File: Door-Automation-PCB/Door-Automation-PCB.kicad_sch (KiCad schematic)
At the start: 10 parts, among them J1 Conn_01x15_Female, J2 Conn_01x15_Female, J3 Screw_Terminal_01x01, J4 Screw_Terminal_01x01, J5 Screw_Terminal_01x02, J6 Screw_Terminal_01x02, U1 ESP32-DEVKIT-V1, U2 buck_converter, U3 buck_converter

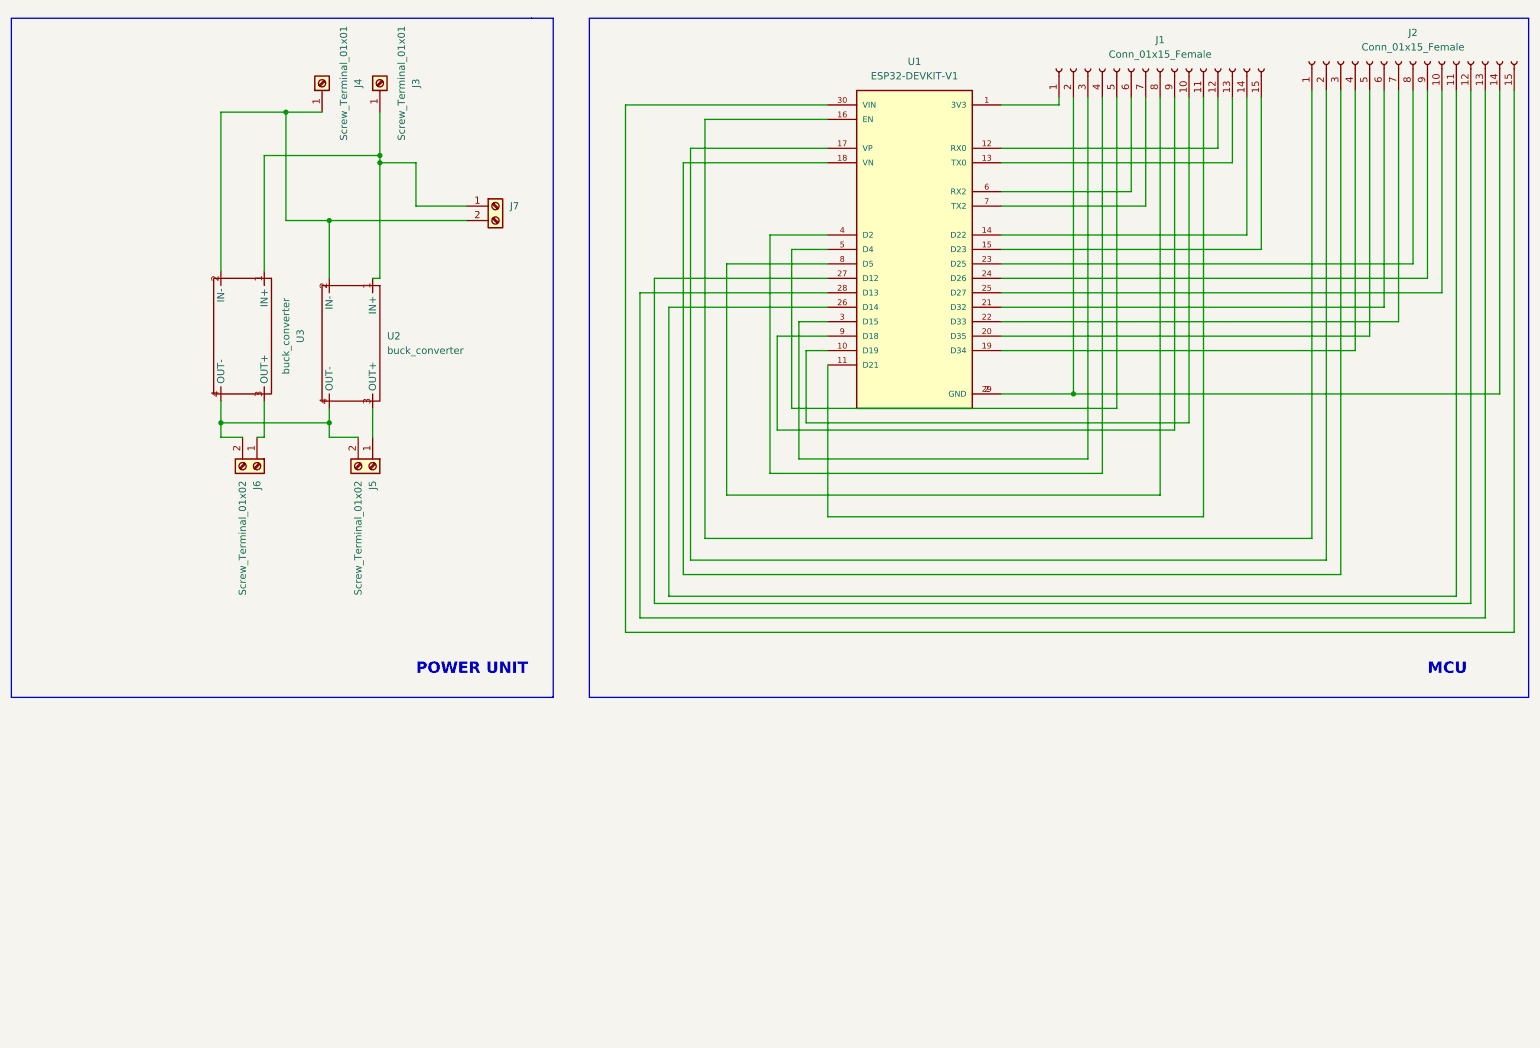
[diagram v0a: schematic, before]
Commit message: added mosfet switch
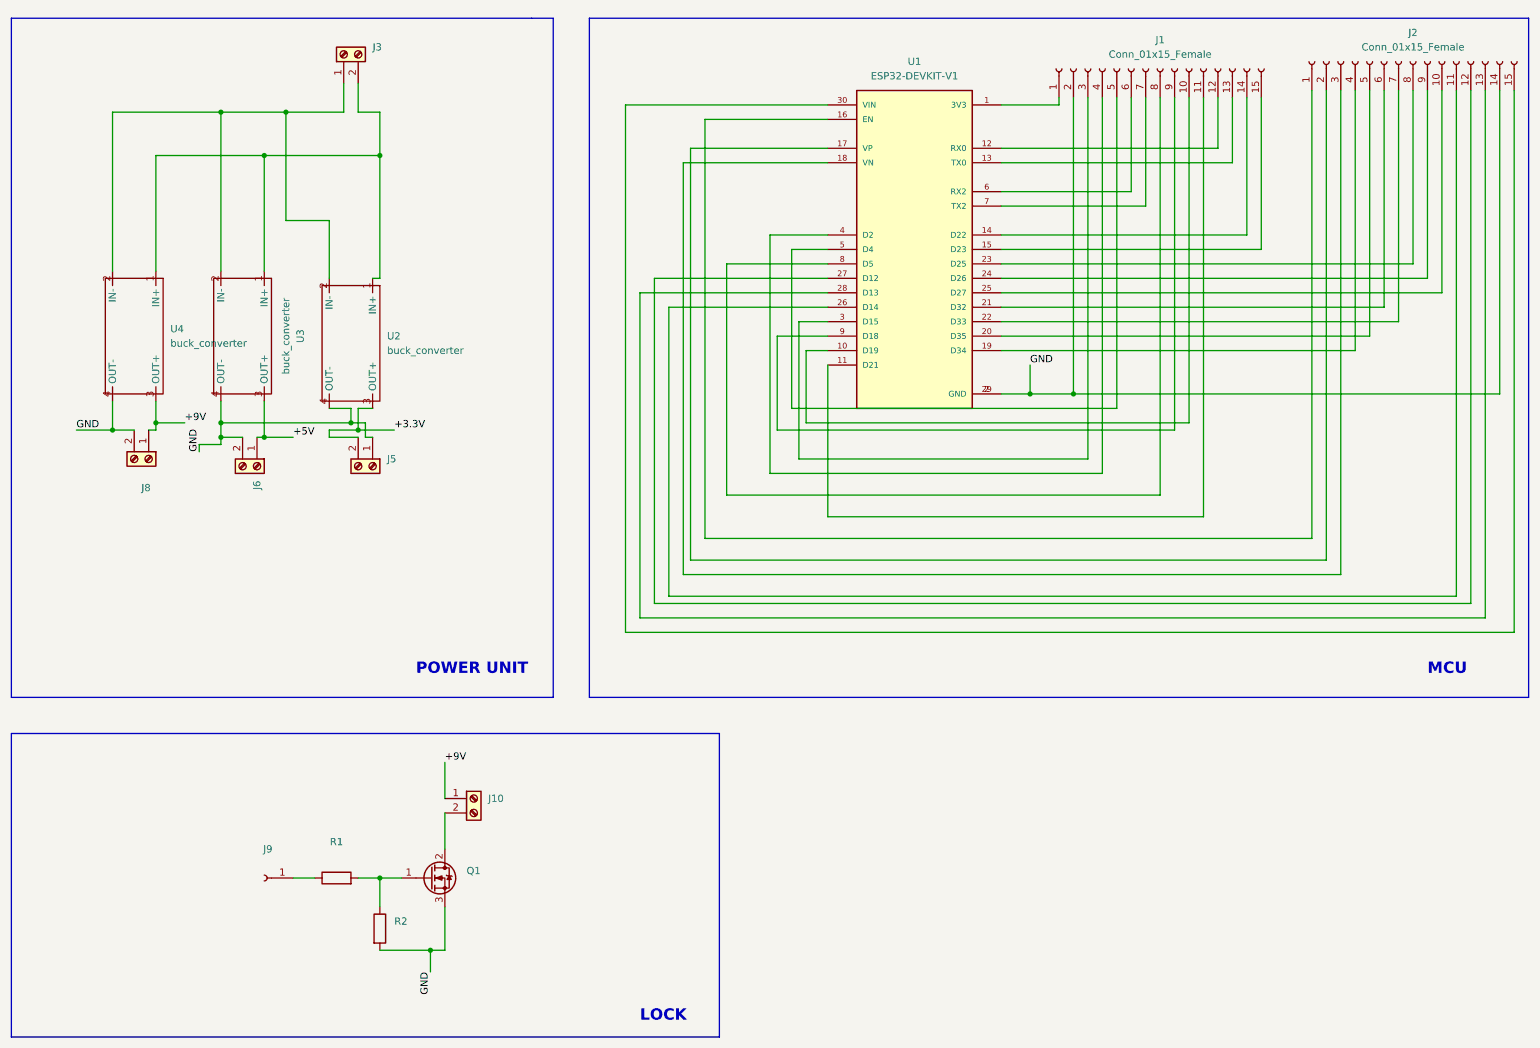
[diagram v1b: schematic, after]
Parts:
- removed J3, J4: Screw_Terminal_01x01, TerminalBlock_MetzConnect:TerminalBlock_MetzConnect_360271_1x01_Horizontal_ScrewM3.0_Boxed, symbol Connector:Screw_Terminal_01x01
- removed J7: (no value), symbol Connector:Screw_Terminal_01x02
- added J10, J3, J8: (no value), symbol Connector:Screw_Terminal_01x02
- added J9: (no value), symbol Connector:Conn_01x01_Female
- added Q1: (no value), symbol Transistor_FET:IRLZ34N
- added R1, R2: (no value), symbol Device:R
- added U4: buck_converter, converters:buck_converter, symbol buck_converter:buck_converter
- J5, J6: value Screw_Terminal_01x02 -> (none); footprint TerminalBlock_Phoenix:TerminalBlock_Phoenix_MKDS-1,5-2-5.08_1x02_P5.08mm_Horizontal -> (none)
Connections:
- net at U2.2 (IN-), U3.2 (IN-): now also J3.1 (Pin_1), U4.2 (IN-)
- net at U2.1 (IN+), U3.1 (IN+): now also J3.2 (Pin_2), U4.1 (IN+)
- net +3.3V: now reaches U2.3 (OUT+)
- net +3.3V: now also J5.2 (Pin_2); no longer J5.1 (Pin_1)
- net GND: now reaches J6.2 (Pin_2), U2.4 (OUT-), U3.4 (OUT-)
- net GND: now also J1.2 (Pin_2), J2.14 (Pin_14), J5.1 (Pin_1), U1.2 (GND), U1.29 (GND), J8.2 (Pin_2), Q1.3 (S), R2.2, U4.4 (OUT-); no longer J5.2 (Pin_2)
- net +5V: now reaches J6.1 (Pin_1), U3.3 (OUT+)
- new net: J9.1 (Pin_1), R1.1
- new net: J10.2 (Pin_2), Q1.2 (D)
- new net: Q1.1 (G), R1.2, R2.1
- new net +9V: J10.1 (Pin_1), J8.1 (Pin_1), U4.3 (OUT+)
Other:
- note added: "LOCK"

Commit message: added drill holes
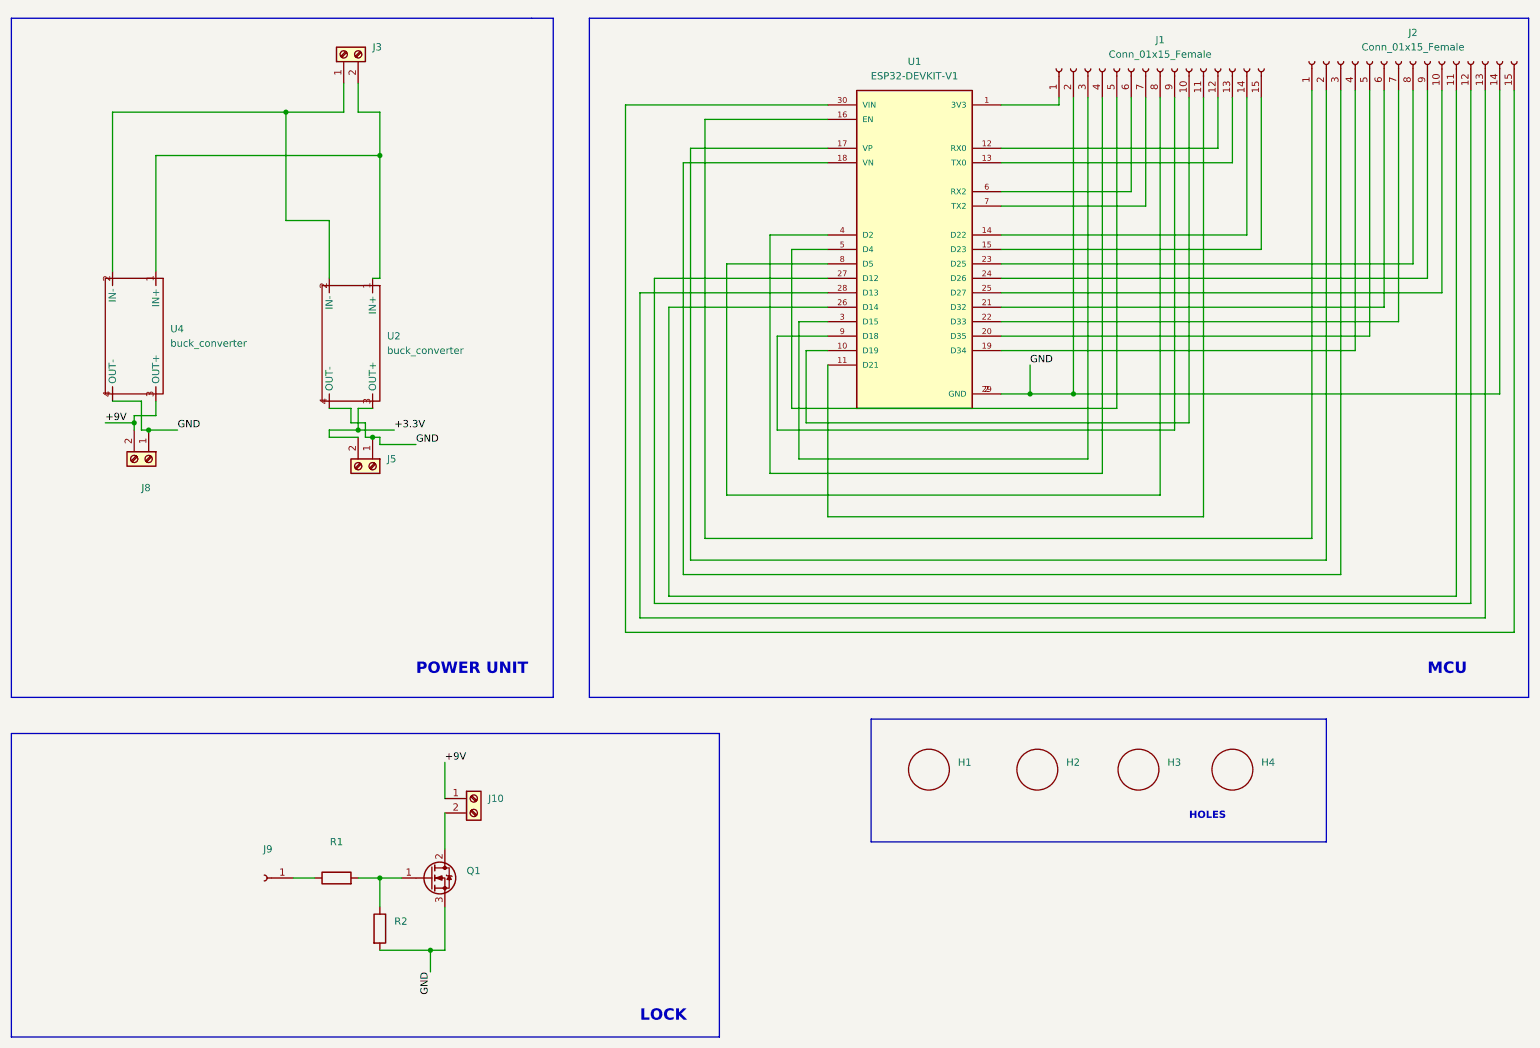
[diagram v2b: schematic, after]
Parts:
- removed J6: (no value), symbol Connector:Screw_Terminal_01x02
- removed U3: buck_converter, converters:buck_converter, symbol buck_converter:buck_converter
- added H1, H2, H3, H4: (no value), symbol drill_hole:hole
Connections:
- net +9V: now also J8.2 (Pin_2); no longer J8.1 (Pin_1)
- net GND: now also J8.1 (Pin_1); no longer J8.2 (Pin_2)
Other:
- note added: "HOLES"

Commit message: routed and added readme
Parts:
- removed H1, H2, H3, H4: (no value), symbol drill_hole:hole
- added H1, H2, H3, H4: MountingHole, MountingHole:MountingHole_2.5mm, symbol Mechanical:MountingHole
- J10: value (none) -> Solenoid conn; footprint (none) -> TerminalBlock_Phoenix:TerminalBlock_Phoenix_MKDS-1,5-2-5.08_1x02_P5.08mm_Horizontal
- J3: value (none) -> 12V_IN; footprint (none) -> TerminalBlock_Phoenix:TerminalBlock_Phoenix_MKDS-1,5-2-5.08_1x02_P5.08mm_Horizontal
- J5: value (none) -> 3.3V; footprint (none) -> TerminalBlock_Phoenix:TerminalBlock_Phoenix_MKDS-1,5-2-5.08_1x02_P5.08mm_Horizontal
- J8: value (none) -> 9V; footprint (none) -> TerminalBlock_Phoenix:TerminalBlock_Phoenix_MKDS-1,5-2-5.08_1x02_P5.08mm_Horizontal
- J9: value (none) -> D; footprint (none) -> Connector_PinSocket_2.00mm:PinSocket_1x01_P2.00mm_Vertical
- Q1: value (none) -> IRLZ34N; footprint (none) -> Package_TO_SOT_THT:TO-220-3_Vertical
- R1: value (none) -> 1K; footprint (none) -> Resistor_THT:R_Axial_DIN0204_L3.6mm_D1.6mm_P7.62mm_Horizontal
- R2: value (none) -> 1OK; footprint (none) -> Resistor_THT:R_Axial_DIN0204_L3.6mm_D1.6mm_P7.62mm_Horizontal
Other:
- note added: "Gearbox Door Automation PCB"
- note added: "MOUNTING HOLES"
- note removed: "HOLES"
